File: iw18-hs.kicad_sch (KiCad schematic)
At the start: 28 parts, among them SW1 SW_SPST, U1 IV-18, U10 TXS0104EPW, U11 MAX811TEUS-T, U3 ESP32-C6-WROOM-1, U8 USBLC6-2P6, U9 DRV8837

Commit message: resistor values
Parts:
- R22, R23: value 100k -> 47k
- R29: value 100k -> 4.7k
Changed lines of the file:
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@@
 			)
 		)
-		(property "Value" "100k"
+		(property "Value" "47k"
 			(at 31.75 121.9199 0)
 			(show_name no)
@@
 			)
 		)
-		(property "Value" "100k"
+		(property "Value" "47k"
 			(at 36.83 146.0499 0)
 			(show_name no)
@@
 			)
 		)
-		(property "Value" "100k"
+		(property "Value" "4.7k"
 			(at 53.34 142.2399 0)
 			(show_name no)

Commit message: sensor heat and some testpoints
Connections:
- net ETANOL_SENSOR_HEAT: now reaches U3.15 (GPIO9)
- no-connect marks 14 -> 13
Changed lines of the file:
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@@
-	)
-	(no_connect
-		(at 139.7 127)
 	)
 	(no_connect
@@
 		(pts
 			(xy 50.8 153.67) (xy 50.8 152.4)
+		)
+		(stroke
+			(width 0)
+			(type default)
+		)
+	)
+	(wire
+		(pts
+			(xy 142.24 127) (xy 139.7 127)
 		)
 		(stroke
@@
 			(hide yes)
 			(show_name no)
+			(do_not_autoplace no)
+			(effects
+				(font
+					(size 1.27 1.27)
+				)
+				(justify left)
+			)
+		)
+	)
+	(global_label "ETANOL_SENSOR_HEAT"
+		(shape input)
+		(at 142.24 127 0)
+		(fields_autoplaced yes)
+		(effects
+			(font
+				(size 1.27 1.27)
+			)
+			(justify left)
+		)
+		(property "Intersheetrefs" "${INTERSHEET_REFS}"
+			(at 166.0894 127 0)
+			(hide yes)
+			(show_name no)

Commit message: Component changes, some new feature
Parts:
- removed C33: 100nF, Capacitor_SMD:C_0805_2012Metric, symbol Device:C
- removed HV5812WG1: HV5812WG, Package_SO:SOIC-28W_7.5x17.9mm_P1.27mm, symbol hv5812:HV5812WG
- removed U1: IV-18, VFD:IV-18, symbol vfd:IV-18
- removed U9: DRV8837, Package_SON:WSON-8-1EP_2x2mm_P0.5mm_EP0.9x1.6mm, symbol Driver_Motor:DRV8837
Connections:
- net ETANOL_SENSOR_HEAT: now also U3.27 (GPIO2/ADC1_CH2); no longer U3.15 (GPIO9)
- no-connect marks 13 -> 6
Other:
- added sheet Powerbank (powerbank.kicad_sch)
- added sheet VFD (vfd.kicad_sch)
- moved on the sheet: C27, R25, R26, SW1, U11

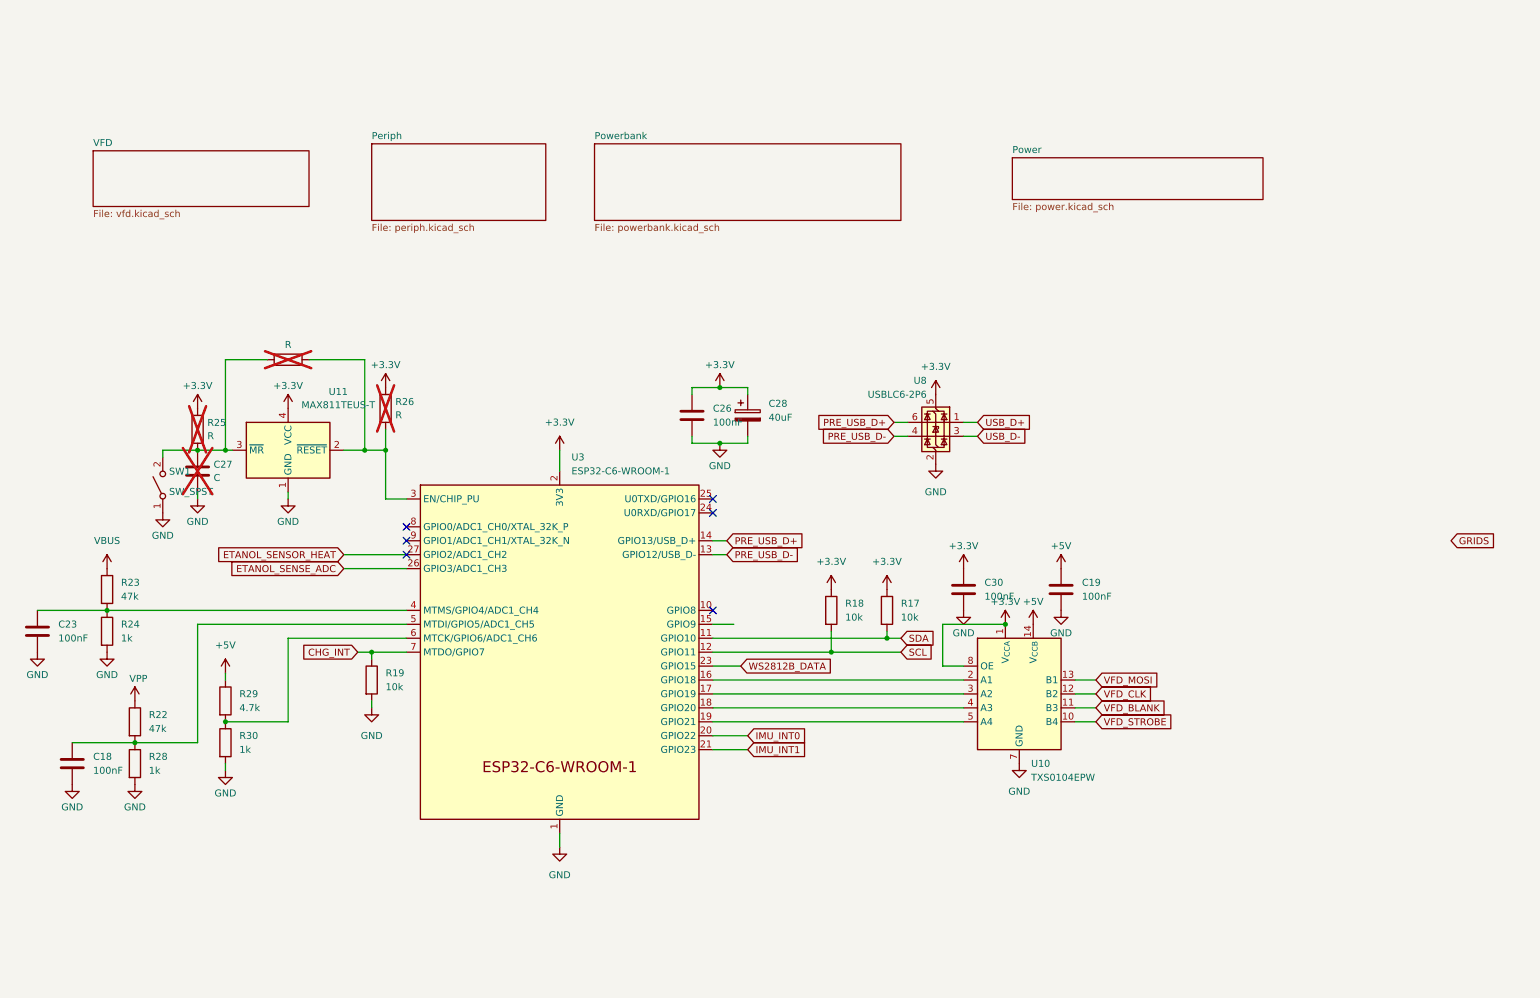
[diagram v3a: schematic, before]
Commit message: Refine board
* Add UART connector for chaining and controll
* shrink the board
workspace 1 output DP-6
* allow for pd controller eeprom programming
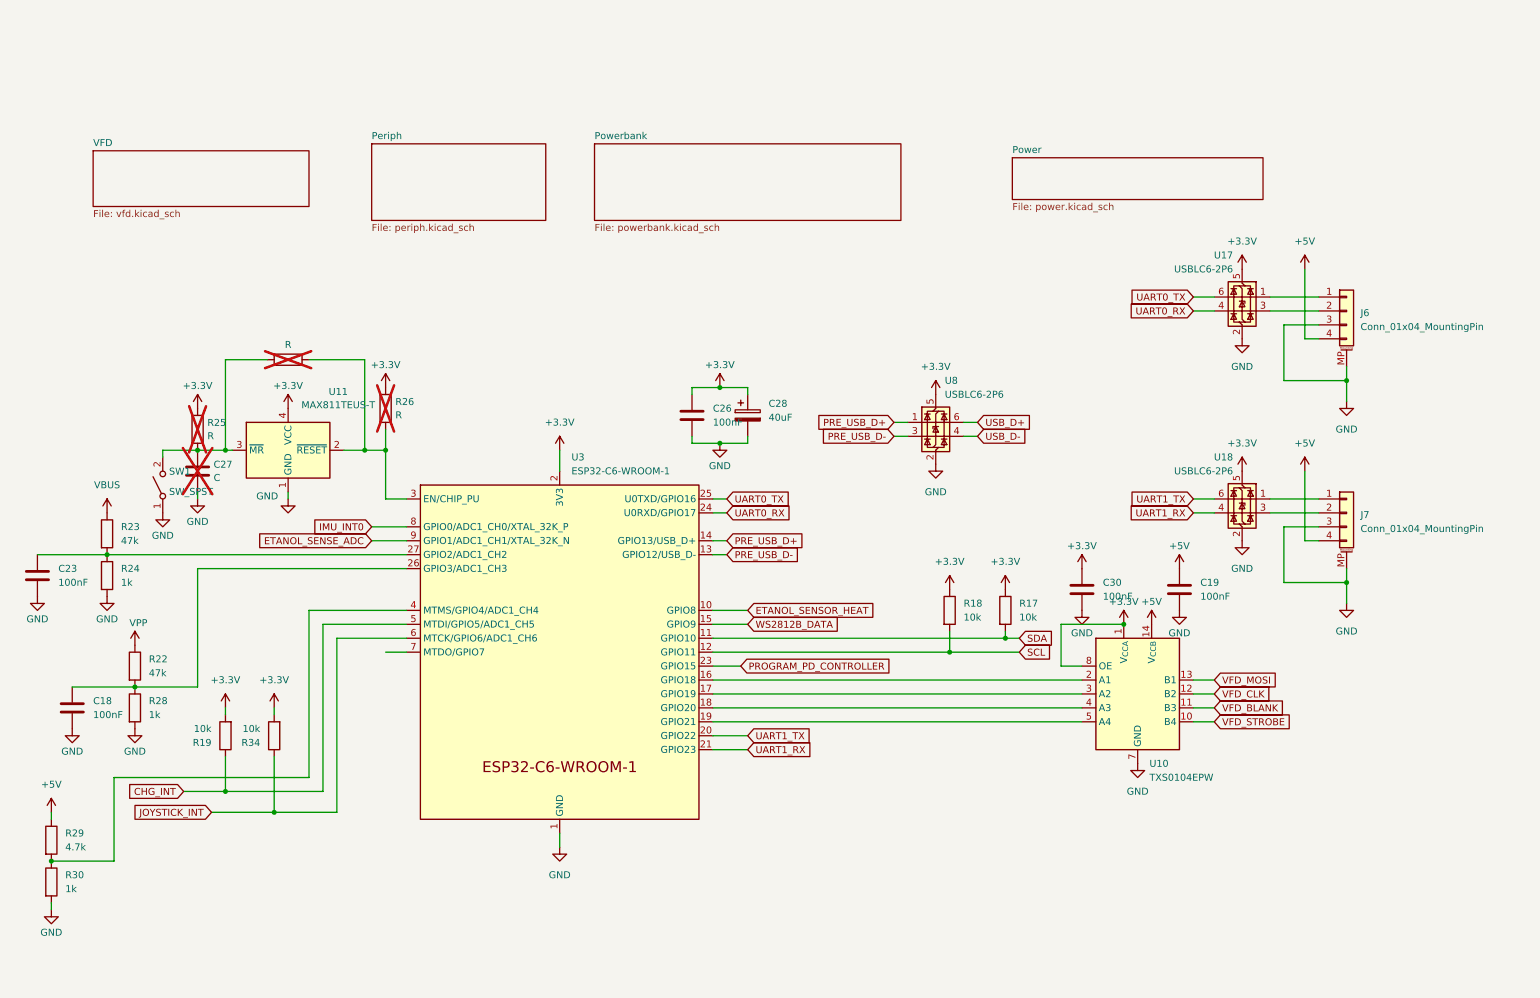
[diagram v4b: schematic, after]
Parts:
- added J6, J7: Conn_01x04_MountingPin, Connector_JST:JST_PH_S4B-PH-SM4-TB_1x04-1MP_P2.00mm_Horizontal, symbol Connector_Generic_MountingPin:Conn_01x04_MountingPin
- added R34: 10k, Resistor_SMD:R_0805_2012Metric, symbol Device:R
- added U17, U18: USBLC6-2P6, Package_TO_SOT_SMD:SOT-666, symbol Power_Protection:USBLC6-2P6
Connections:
- net +3.3V: now also R19.2, R34.2, U17.5 (VBUS), U18.5 (VBUS)
- net +5V: now also J6.4 (Pin_4), J7.4 (Pin_4)
- net CHG_INT: now also U3.5 (MTDI/GPIO5/ADC1_CH5); no longer U3.7 (MTDO/GPIO7)
- net ETANOL_SENSE_ADC: now also U3.9 (GPIO1/ADC1_CH1/XTAL_32K_N); no longer U3.26 (GPIO3/ADC1_CH3)
- net ETANOL_SENSOR_HEAT: now also U3.10 (GPIO8); no longer U3.27 (GPIO2/ADC1_CH2)
- net GND: now also J6.3 (Pin_3), J6.MP (MountPin), J7.3 (Pin_3), J7.MP (MountPin), U17.2 (GND), U18.2 (GND); no longer R19.2
- net IMU_INT0: now also U3.8 (GPIO0/ADC1_CH0/XTAL_32K_P); no longer U3.20 (GPIO22)
- net PRE_USB_D+: now also U8.1 (I/O1); no longer U8.6 (I/O1)
- net PRE_USB_D-: now also U8.3 (I/O2); no longer U8.4 (I/O2)
- net USB_D+: now also U8.6 (I/O1); no longer U8.1 (I/O1)
- net USB_D-: now also U8.4 (I/O2); no longer U8.3 (I/O2)
- net WS2812B_DATA: now also U3.15 (GPIO9); no longer U3.23 (GPIO15)
- net at R29.2, R30.1: now also U3.4 (MTMS/GPIO4/ADC1_CH4); no longer U3.6 (MTCK/GPIO6/ADC1_CH6)
- net at C23.1, R23.2, R24.1: now also U3.27 (GPIO2/ADC1_CH2); no longer U3.4 (MTMS/GPIO4/ADC1_CH4)
- net at C18.1, R22.2, R28.1: now also U3.26 (GPIO3/ADC1_CH3); no longer U3.5 (MTDI/GPIO5/ADC1_CH5)
- net UART0_RX: now reaches U3.24 (U0RXD/GPIO17)
- net UART0_RX: now also U17.4 (I/O2)
- net UART0_TX: now reaches U3.25 (U0TXD/GPIO16)
- net UART0_TX: now also U17.6 (I/O1)
- net IMU_INT1 renamed UART1_RX
- net UART1_RX: now also U18.4 (I/O2)
- new net: J6.1 (Pin_1), U17.1 (I/O1)
- new net: J6.2 (Pin_2), U17.3 (I/O2)
- new net: J7.1 (Pin_1), U18.1 (I/O1)
- new net: J7.2 (Pin_2), U18.3 (I/O2)
- new net JOYSTICK_INT: R34.1, U3.6 (MTCK/GPIO6/ADC1_CH6)
- new net PROGRAM_PD_CONTROLLER: U3.23 (GPIO15)
- new net UART1_TX: U18.6 (I/O1), U3.20 (GPIO22)
- no-connect marks 6 -> 0
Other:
- moved on the sheet: C18, C19, C23, C30, R17, R18, R19, R22, R23, R24, R28, R29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

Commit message: Add mounting holes and put test points
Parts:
- added H1, H2: MountingHole_Pad, MountingHole:MountingHole_4.3mm_M4_Pad_Via, symbol Mechanical:MountingHole_Pad
- added H3, H4, H5, H6: MountingHole_Pad, MountingHole:MountingHole_2.2mm_M2_Pad_Via, symbol Mechanical:MountingHole_Pad
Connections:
- net GND: now also H1.1, H2.1, H3.1, H4.1, H5.1, H6.1
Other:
- moved on the sheet: C18, C19, C23, C26, C27, C28, C30, J6, J7, R17, R18, R19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

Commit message: Start routing
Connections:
- net UART0_RX: now also U17.3 (I/O2); no longer U17.4 (I/O2)
- net UART0_TX: now also U17.1 (I/O1); no longer U17.6 (I/O1)
- net UART1_RX: now also U18.3 (I/O2); no longer U18.4 (I/O2)
- net UART1_TX: now also U18.1 (I/O1); no longer U18.6 (I/O1)
- net at J6.1 (Pin_1): now also U17.6 (I/O1); no longer U17.1 (I/O1)
- net at J6.2 (Pin_2): now also U17.4 (I/O2); no longer U17.3 (I/O2)
- net at J7.1 (Pin_1): now also U18.6 (I/O1); no longer U18.1 (I/O1)
- net at J7.2 (Pin_2): now also U18.4 (I/O2); no longer U18.3 (I/O2)
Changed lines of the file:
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@@
 		(lib_id "Power_Protection:USBLC6-2P6")
 		(at 238.76 48.26 0)
-		(mirror y)
 		(unit 1)
 		(body_style 1)
@@
 		(dnp no)
 		(property "Reference" "U17"
-			(at 237.1089 40.64 0)
+			(at 240.4111 40.64 0)
 			(show_name no)
 			(do_not_autoplace no)
@@
 		)
 		(property "Value" "USBLC6-2P6"
-			(at 237.1089 43.18 0)
+			(at 240.4111 43.18 0)
 			(show_name no)
 			(do_not_autoplace no)
@@
 		)
 		(property "Footprint" "Package_TO_SOT_SMD:SOT-666"
-			(at 237.744 54.991 0)
+			(at 239.776 54.991 0)
 			(hide yes)
 			(show_name no)
@@
 		)
 		(property "Datasheet" "https://www.st.com/resource/en/datasheet/usblc6-2.pdf"
-			(at 237.744 56.896 0)
+			(at 239.776 56.896 0)
 			(hide yes)
 			(show_name no)
@@
 		(lib_id "Power_Protection:USBLC6-2P6")
 		(at 238.76 85.09 0)
-		(mirror y)
 		(unit 1)
 		(body_style 1)
@@
 		(dnp no)
 		(property "Reference" "U18"
-			(at 237.1089 77.47 0)
+			(at 240.4111 77.47 0)
 			(show_name no)
 			(do_not_autoplace no)
@@
 		)
 		(property "Value" "USBLC6-2P6"
-			(at 237.1089 80.01 0)
+			(at 240.4111 80.01 0)
 			(show_name no)
 			(do_not_autoplace no)
@@
 		)
 		(property "Footprint" "Package_TO_SOT_SMD:SOT-666"
-			(at 237.744 91.821 0)
+			(at 239.776 91.821 0)
 			(hide yes)
 			(show_name no)
@@
 		)
 		(property "Datasheet" "https://www.st.com/resource/en/datasheet/usblc6-2.pdf"
-			(at 237.744 93.726 0)
-			(hide yes)
-			(show_name no)
+			(at 239.776 93.726 0)
+			(hide yes)
+			(show_name no)

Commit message: Route some
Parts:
- added JP1, JP2: SolderJumper_2_Open, Jumper:SolderJumper-2_P1.3mm_Open_RoundedPad1.0x1.5mm, symbol Jumper:SolderJumper_2_Open
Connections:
- net +5V: no longer J6.4 (Pin_4), J7.4 (Pin_4)
- net ETANOL_SENSE_ADC: now also U3.8 (GPIO0/ADC1_CH0/XTAL_32K_P); no longer U3.9 (GPIO1/ADC1_CH1/XTAL_32K_N)
- net IMU_INT0: now also U3.9 (GPIO1/ADC1_CH1/XTAL_32K_N); no longer U3.8 (GPIO0/ADC1_CH0/XTAL_32K_P)
- net F_PWM: now reaches U3.7 (MTDO/GPIO7)
- net PROGRAM_PD_CONTROLLER renamed F_EN
- new net: J6.4 (Pin_4), JP1.1 (A)
- new net: J7.4 (Pin_4), JP2.1 (A)
- new net VBUS_FUSED: JP1.2 (B), JP2.2 (B)
